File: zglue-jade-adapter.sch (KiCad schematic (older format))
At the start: 66 parts, among them J1 543630489, J2 543630489, U1 zGlue-Jade

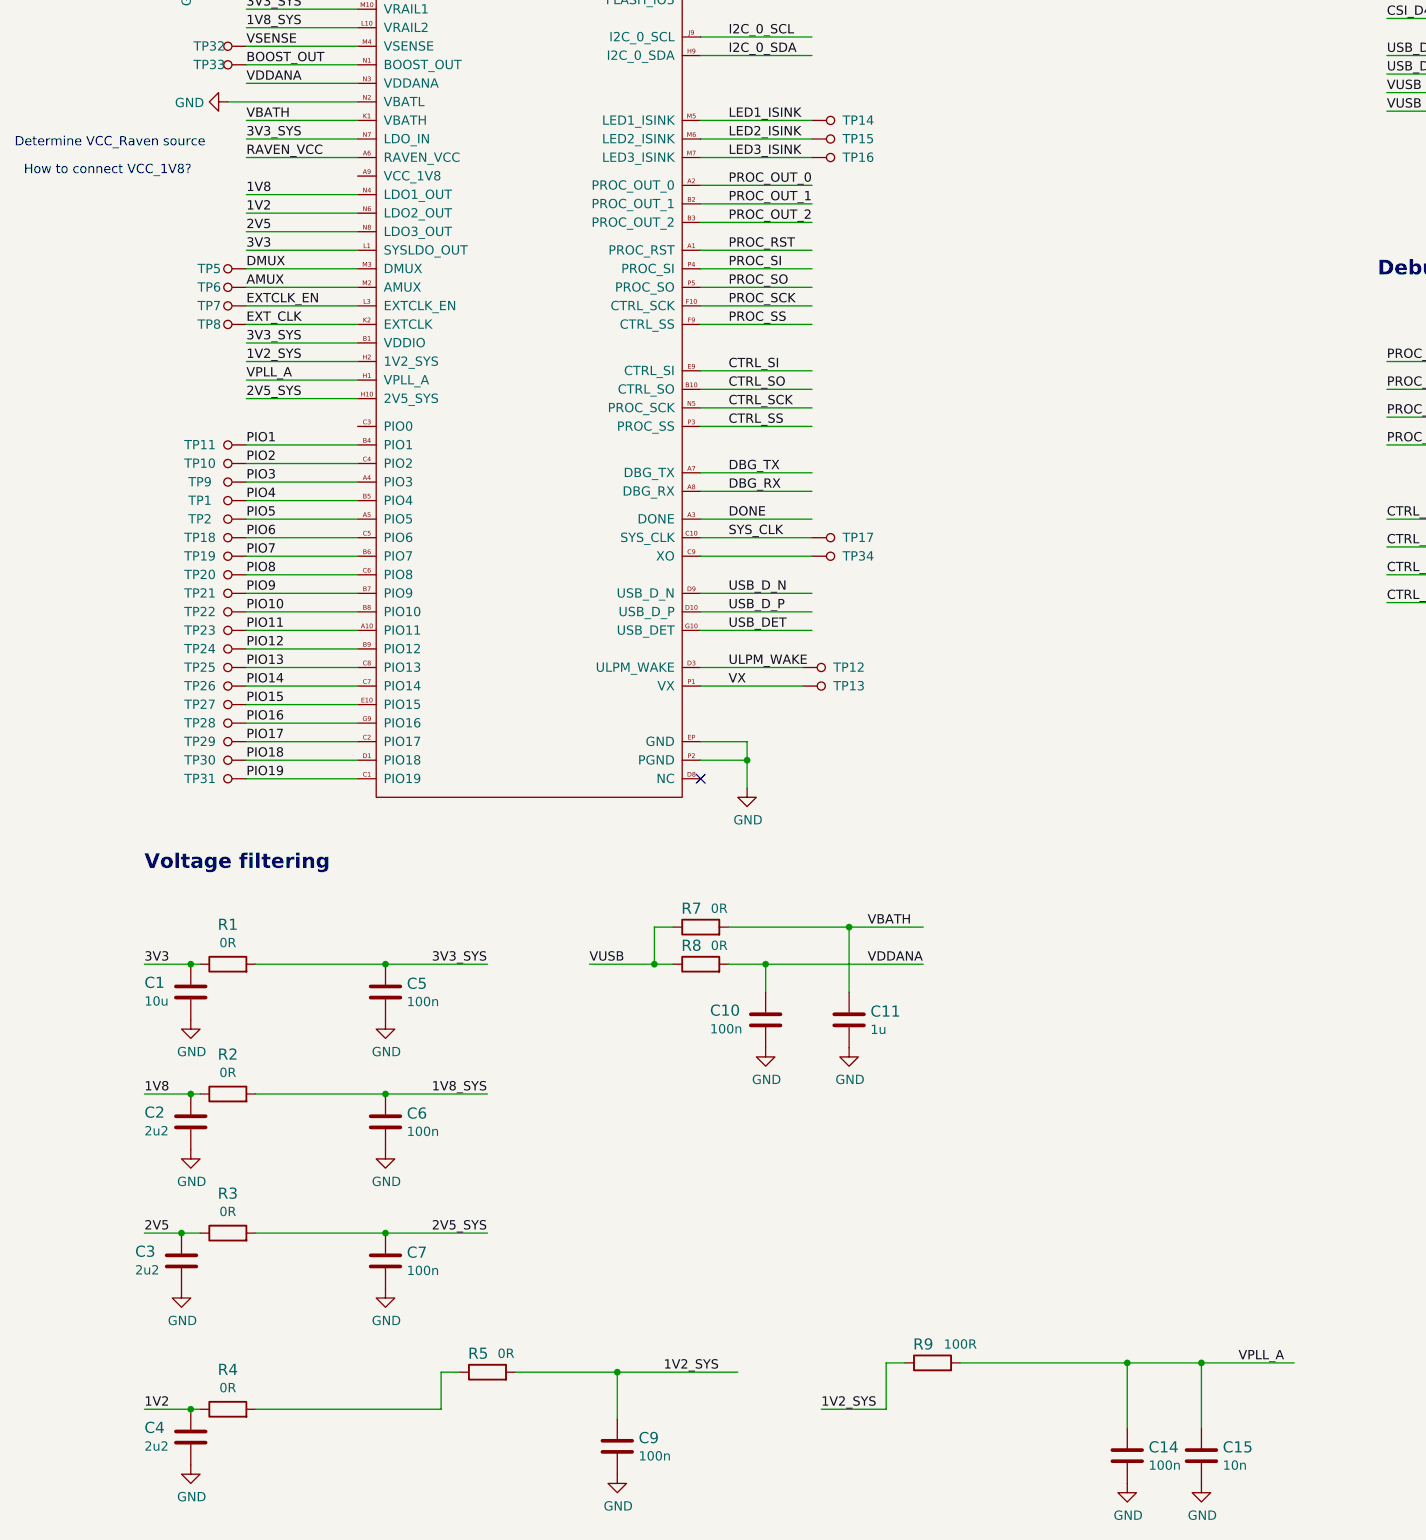
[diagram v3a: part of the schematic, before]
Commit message: Add 3D Vis to README
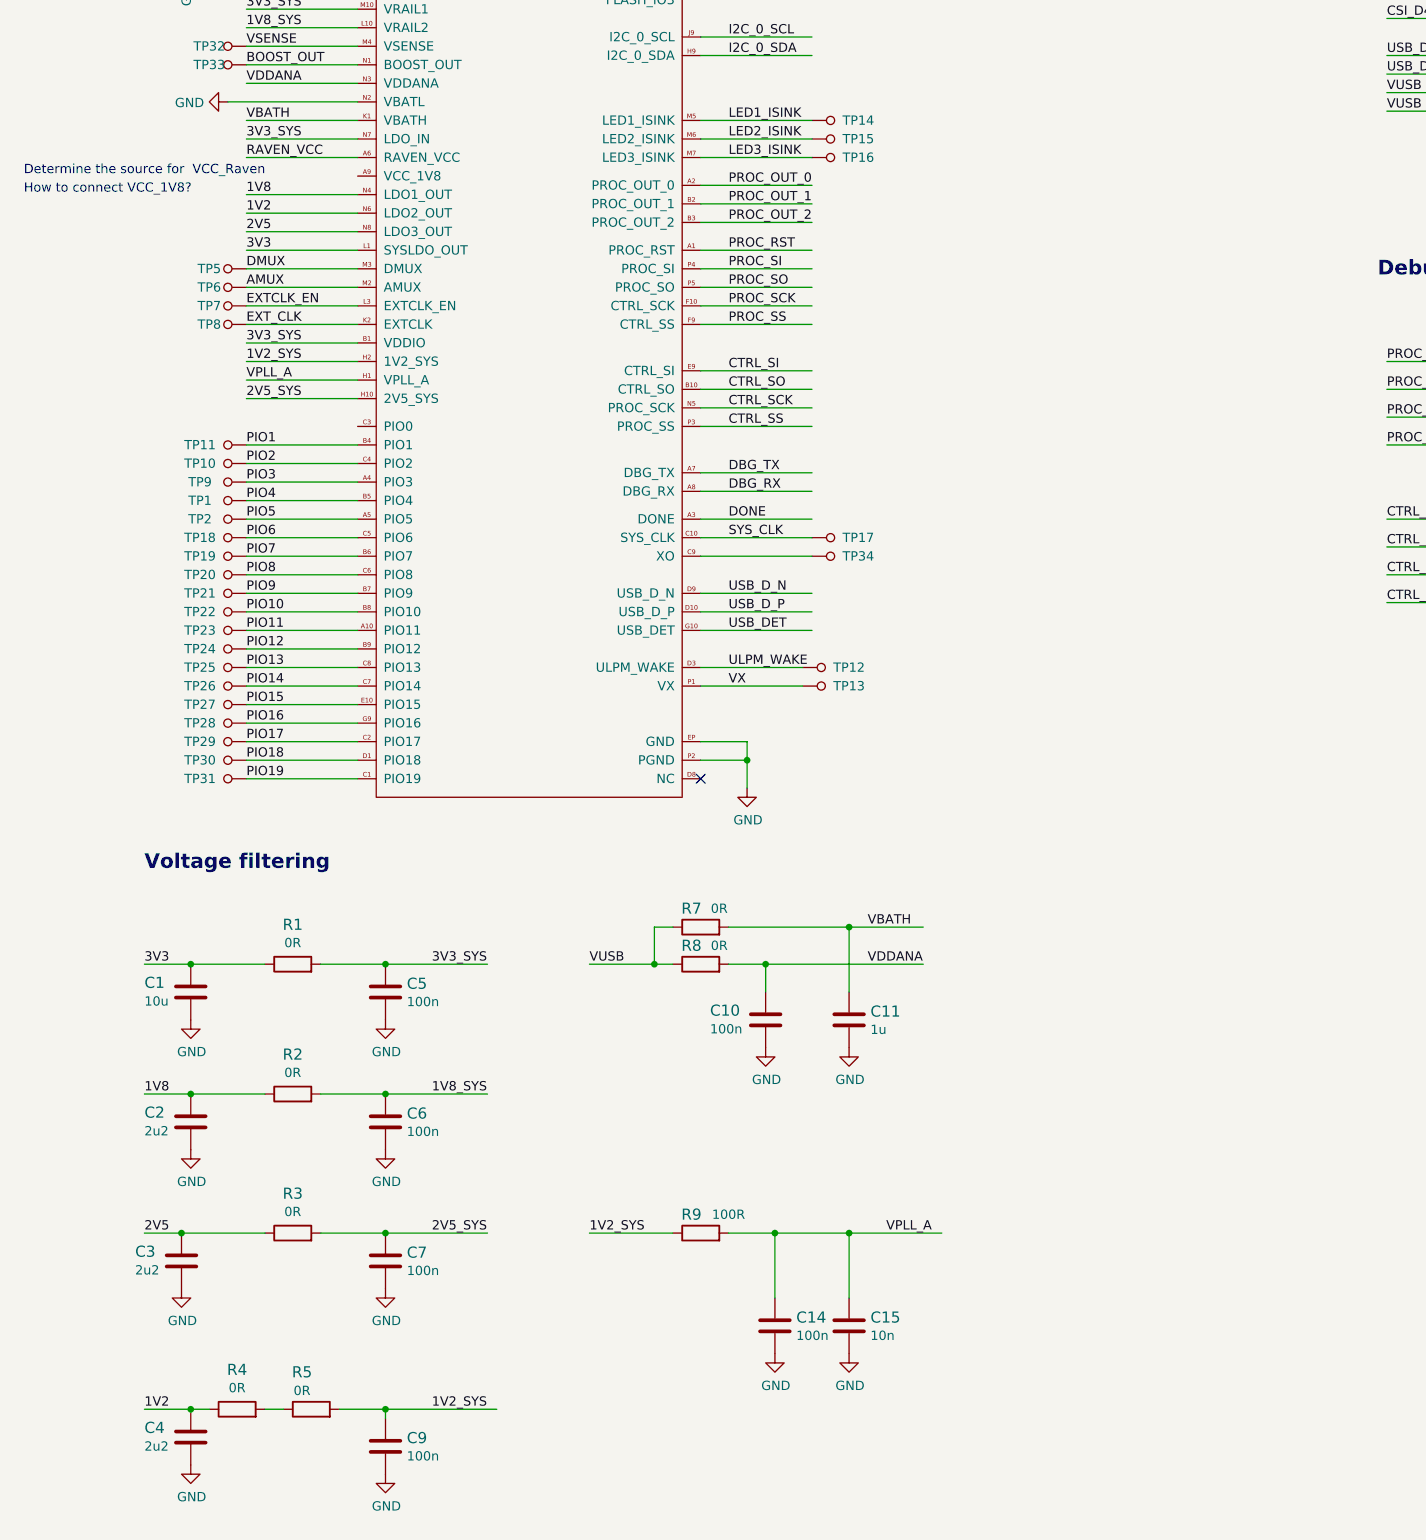
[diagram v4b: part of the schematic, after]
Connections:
- wire segments 249 -> 245
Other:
- note added: "Determine the source for VCC_Raven"
- note removed: "Determine VCC_Raven source"
- moved on the sheet: C14, C15, C9, R1, R2, R3, R4, R5, R9

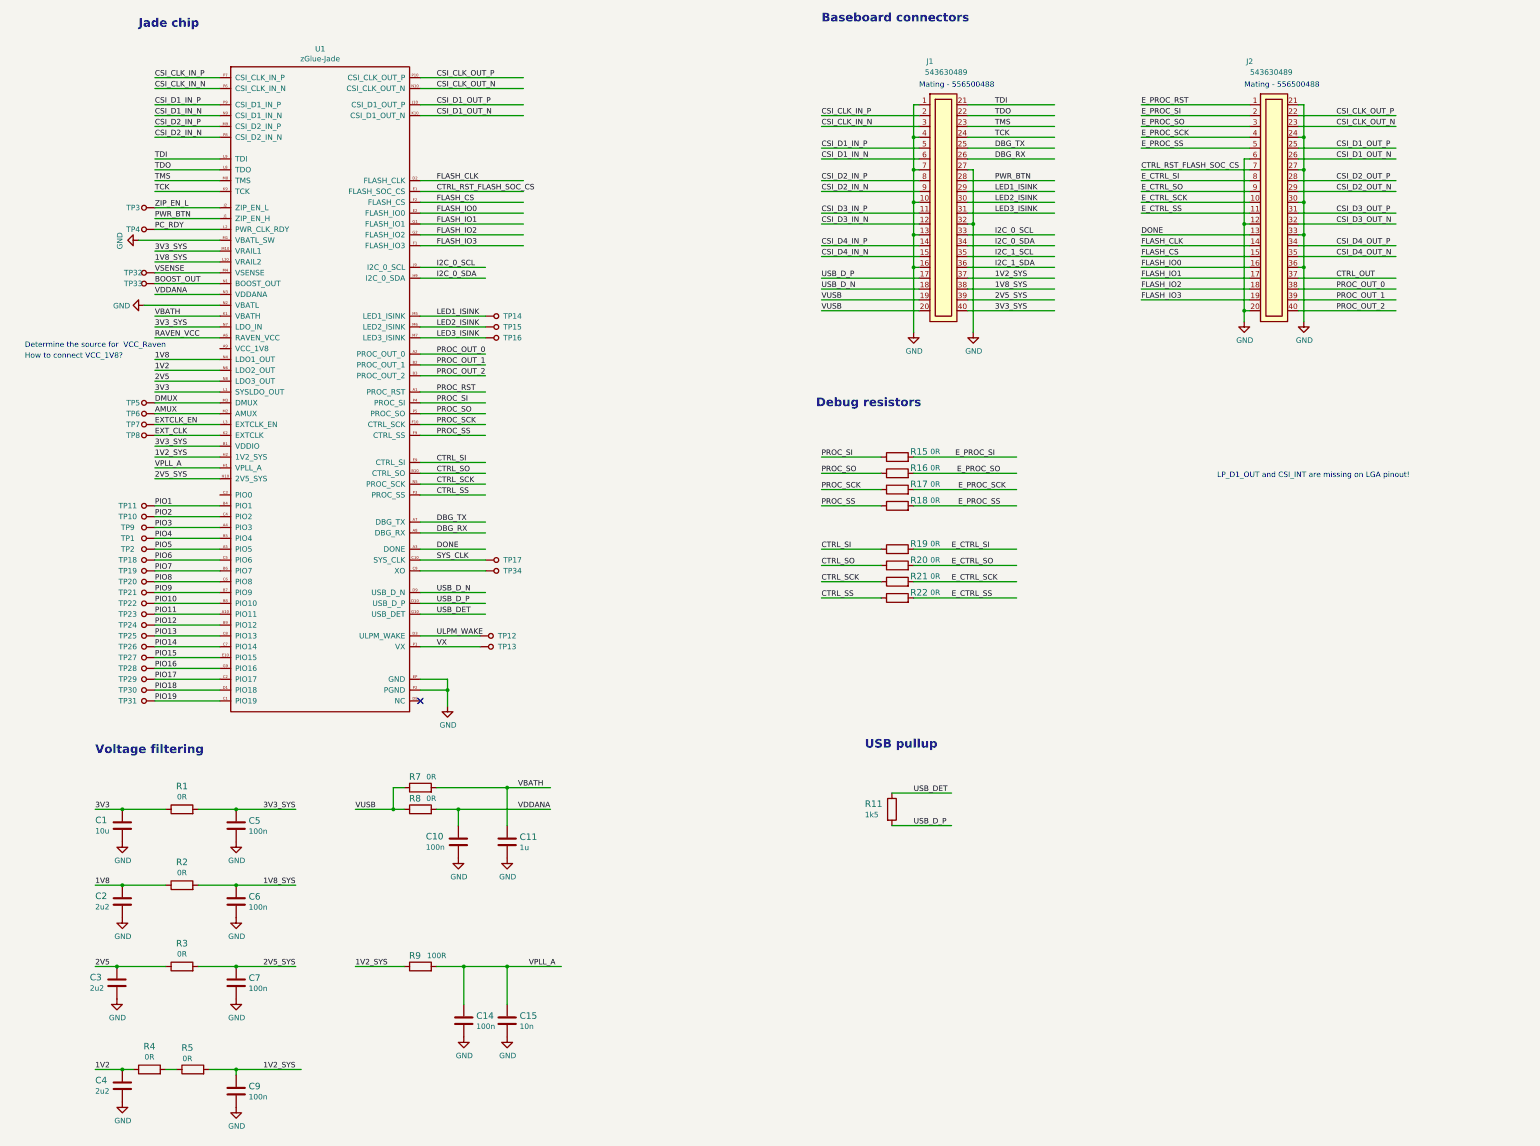
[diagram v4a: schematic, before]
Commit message: Add CSI_LP and CSI_INT signals and corresponding resistors
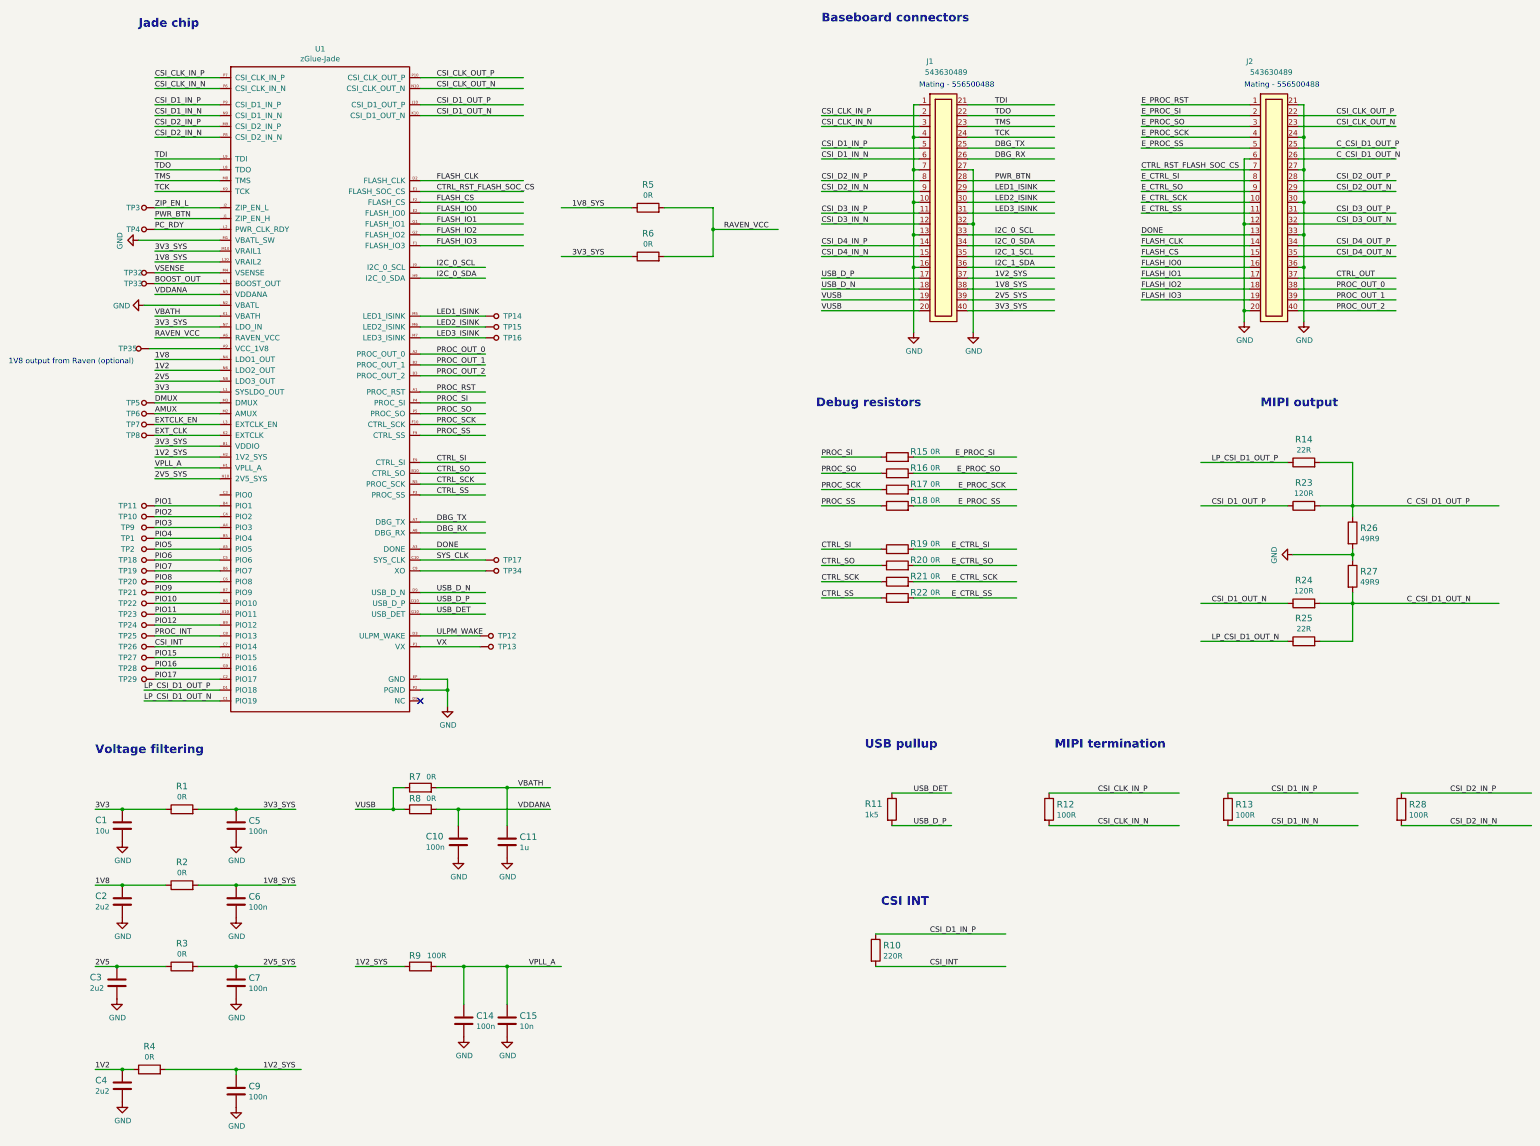
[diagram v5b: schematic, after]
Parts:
- removed TP30, TP31: TP_SMD1MM, antmicro-footprints:Testpoint_smd_1mm, symbol antmicroTestPoints:TP_SMD1MM
- added R10: R_220R_0402, antmicro-footprints:0402-res, symbol antmicroResistors0402:R_220R_0402
- added R12, R13, R28: R_100R_0402, antmicro-footprints:0402-res, symbol antmicroResistors0402:R_100R_0402
- added R14, R25: R_22R_0402, antmicro-footprints:0402-res, symbol antmicroResistors0402:R_22R_0402
- added R23, R24: R_120R_0402, antmicro-footprints:0402-res, symbol antmicroResistors0402:R_100R_0402
- added R26, R27: R_49R9_0402, antmicro-footprints:0402-res, symbol antmicroResistors0402:R_49R9_0402
- added R6: R_0R_0402, antmicro-footprints:0402-res, symbol antmicroResistors0402:R_0R_0402
- added TP35: TP_SMD1MM, antmicro-footprints:Testpoint_smd_1mm, symbol antmicroTestPoints:TP_SMD1MM
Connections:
- net labels added: CSI_INT, C_CSI_D1_OUT_N, C_CSI_D1_OUT_P, LP_CSI_D1_OUT_N, LP_CSI_D1_OUT_P, PROC_INT
- net labels removed: PIO13, PIO14, PIO18, PIO19
- wire segments 245 -> 277
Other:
- note added: "1V8 output from Raven (optional)"
- note added: "CSI INT"
- note added: "MIPI output"
- note added: "MIPI termination"
- note removed: "Determine the source for VCC_Raven"
- note removed: "How to connect VCC_1V8?"
- note removed: "LP_D1_OUT and CSI_INT are missing on LGA pinout!"

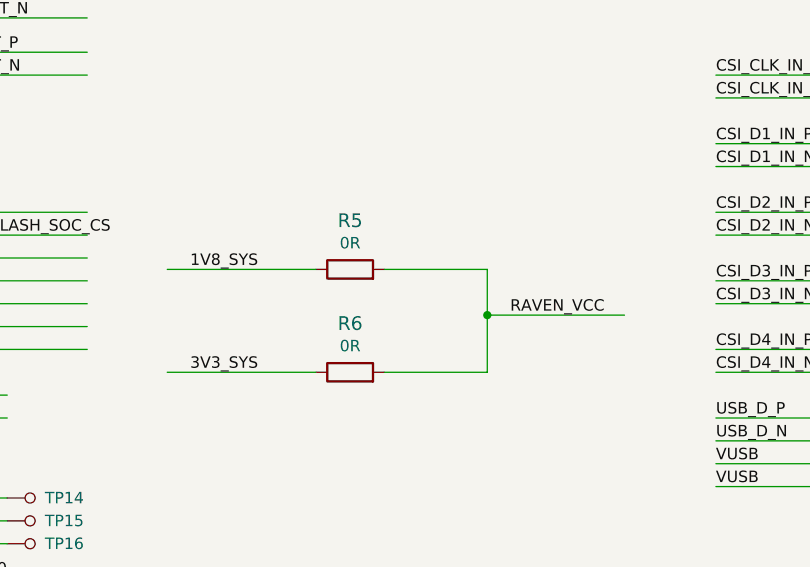
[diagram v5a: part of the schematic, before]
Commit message: Add DNP annotations
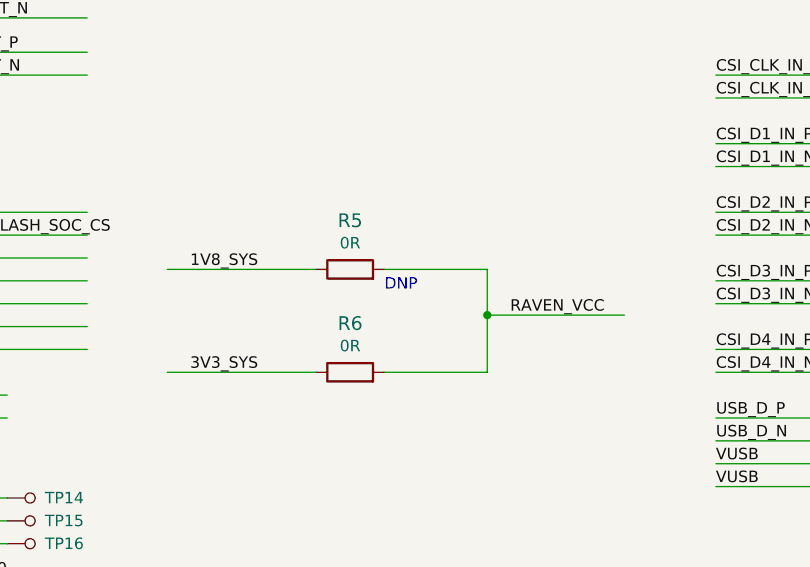
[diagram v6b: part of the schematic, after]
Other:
- note added: "DNP"
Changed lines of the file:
@@
 Text Label 1650 7050 0    50   ~ 0
 LP_CSI_D1_OUT_N
+Text Notes 6450 2600 0    50   ~ 0
+DNP
 $EndSCHEMATC
